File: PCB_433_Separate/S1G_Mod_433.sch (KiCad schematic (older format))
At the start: 18 parts

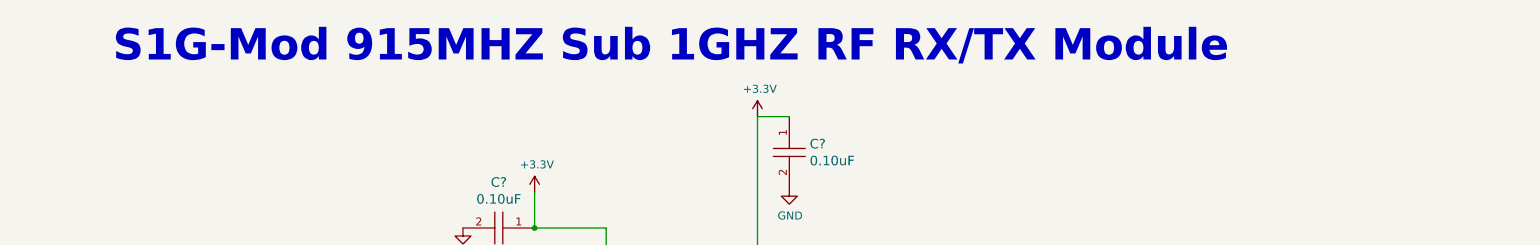
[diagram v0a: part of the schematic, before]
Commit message: Progress and reorganized
project reorganized separate PA/LNA version near done, added an M0+ MCU.
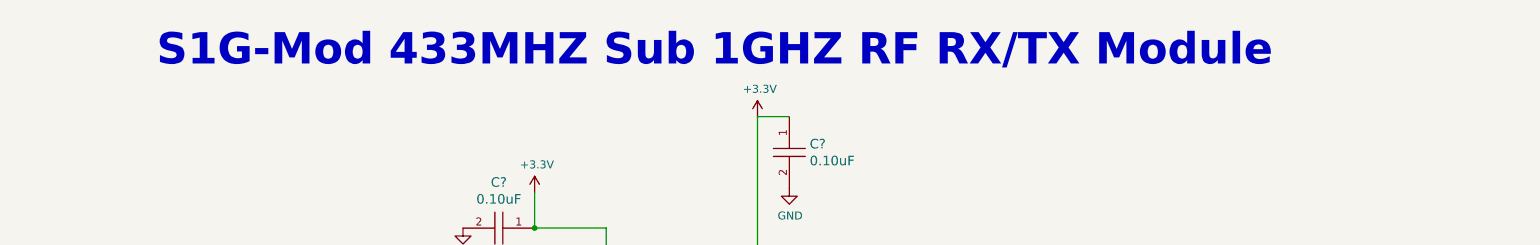
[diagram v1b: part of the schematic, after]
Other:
- note added: "S1G-Mod 433MHZ Sub 1GHZ RF RX/TX Module"
- note removed: "S1G-Mod 915MHZ Sub 1GHZ RF RX/TX Module"
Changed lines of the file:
@@
 	1    0    0    -1
 $EndComp
-Text Notes 2375 975  0    197  ~ 39
-S1G-Mod 915MHZ Sub 1GHZ RF RX/TX Module
+Text Notes 2650 1000 0    197  ~ 39
+S1G-Mod 433MHZ Sub 1GHZ RF RX/TX Module
 $EndSCHEMATC
